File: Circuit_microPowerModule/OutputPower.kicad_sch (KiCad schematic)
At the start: 61 parts, among them J101 Screw_Terminal_01x02, J401 Conn_01x03, Q401 RU1C002ZP, Q402 RK7002BM, Q403 RU1C002ZP, Q404 RK7002BM, U301 OPA376xxDBV, U401 MP2315S, U407 L298N

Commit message: update system power circuit layout
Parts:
- C409, C410: footprint Capacitor_SMD:C_1206_3216Metric -> Capacitor_SMD:C_1210_3225Metric
- L402: footprint Inductor_SMD_Wurth:L_Wurth_WE-LQSH-2512 -> Inductor_SMD:L_Sunlord_MWSA1204S-4R7
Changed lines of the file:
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@@
       (effects (font (size 1.27 1.27)) (justify left))
     )
-    (property "Footprint" "Capacitor_SMD:C_1206_3216Metric" (at 144.78 71.12 0)
+    (property "Footprint" "Capacitor_SMD:C_1210_3225Metric" (at 144.78 71.12 0)
       (effects (font (size 1.27 1.27)) hide)
     )
@@
       (effects (font (size 1.27 1.27)))
     )
-    (property "Footprint" "Inductor_SMD_Wurth:L_Wurth_WE-LQSH-2512" (at 121.92 68.58 0)
+    (property "Footprint" "Inductor_SMD:L_Sunlord_MWSA1204S-4R7" (at 121.92 68.58 0)
       (effects (font (size 1.27 1.27)) hide)
     )
@@
       (effects (font (size 1.27 1.27)) (justify left))
     )
-    (property "Footprint" "Capacitor_SMD:C_1206_3216Metric" (at 128.27 71.12 0)
-      (effects (font (size 1.27 1.27)) hide)
-    )
+    (property "Footprint" "Capacitor_SMD:C_1210_3225Metric" (at 128.27 71.12 0)
+      (effects (font (size 1.27 1.27)) hide)
+    )

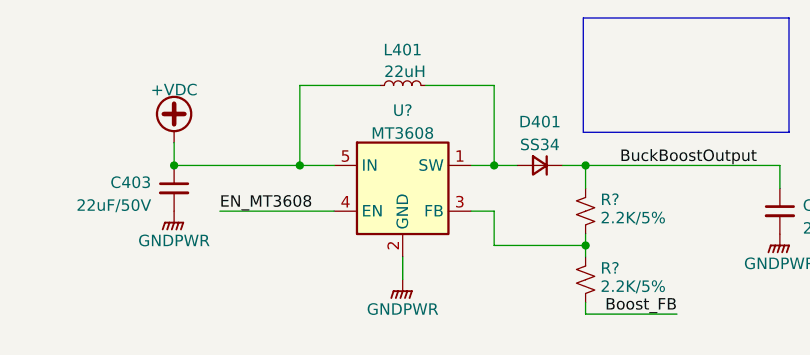
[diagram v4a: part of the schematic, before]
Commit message: update output inductor footprint
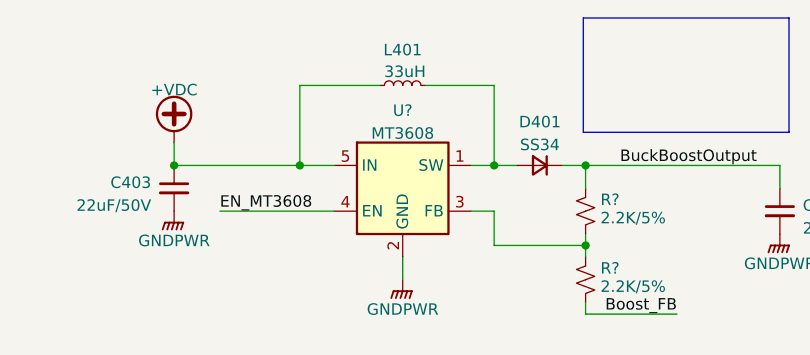
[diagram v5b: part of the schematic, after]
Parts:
- L401: value 22uH -> 33uH; footprint Inductor_SMD_Wurth:L_Wurth_WE-LQSH-2512 -> Inductor_SMD:L_Bourns-SRU1028_10.0x10.0mm
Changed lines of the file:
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@@
       (effects (font (size 1.27 1.27)))
     )
-    (property "Value" "22uH" (at 81.534 23.876 90)
+    (property "Value" "33uH" (at 81.534 23.876 90)
       (effects (font (size 1.27 1.27)))
     )
-    (property "Footprint" "Inductor_SMD_Wurth:L_Wurth_WE-LQSH-2512" (at 81.28 25.4 0)
+    (property "Footprint" "Inductor_SMD:L_Bourns-SRU1028_10.0x10.0mm" (at 81.28 25.4 0)
       (effects (font (size 1.27 1.27)) hide)
     )

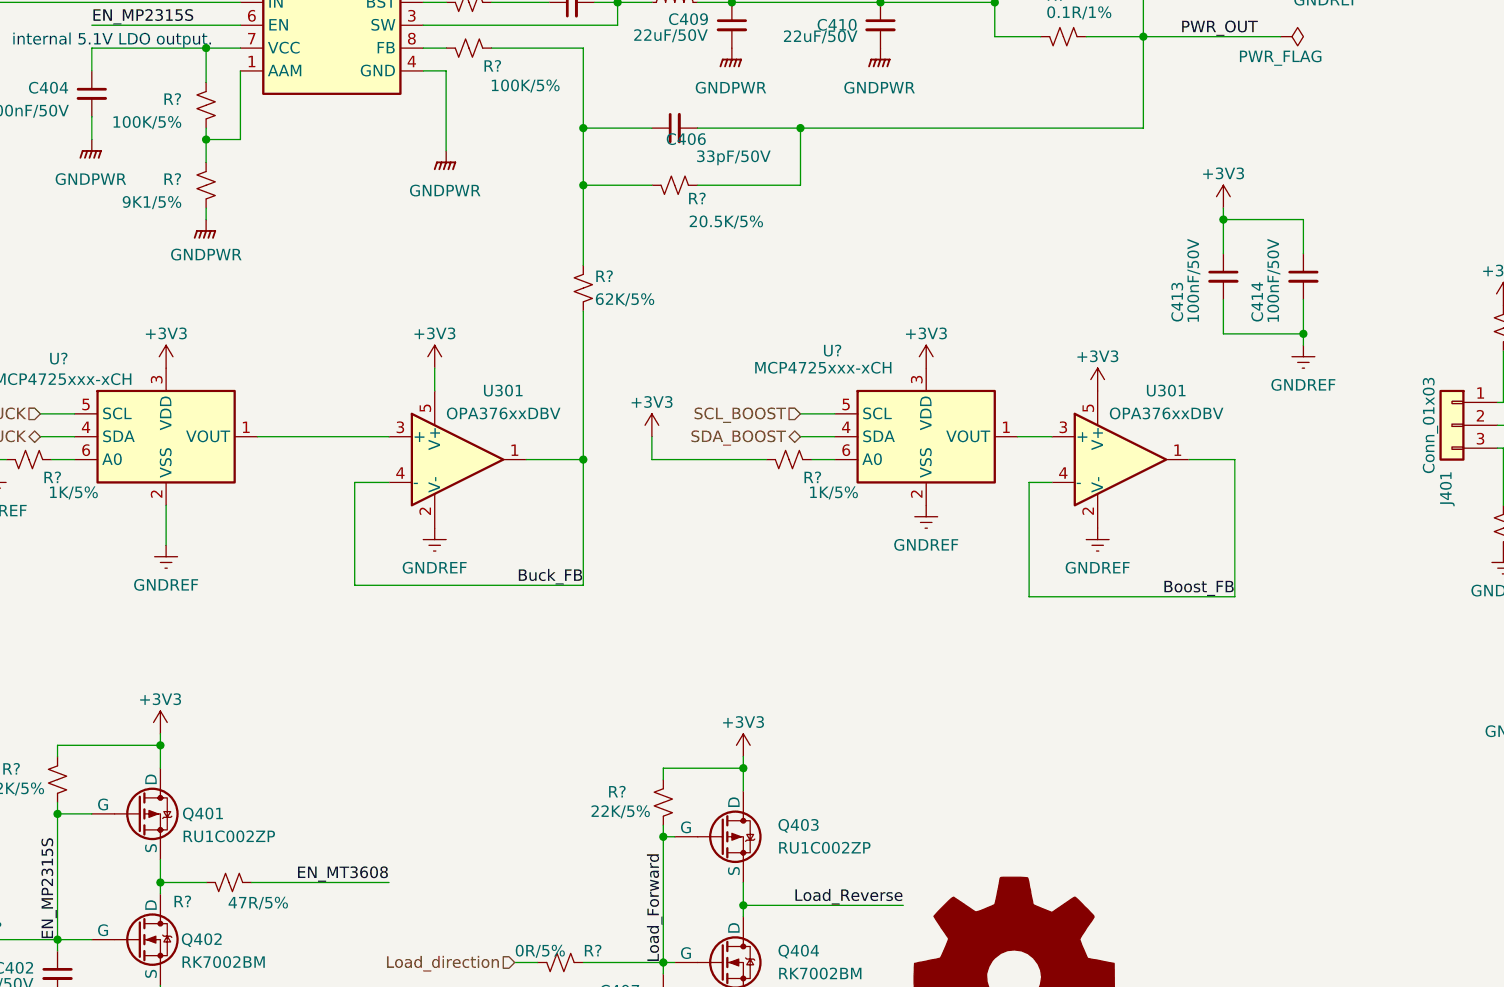
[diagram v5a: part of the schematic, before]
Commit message: modify DAC to Voltage follwers
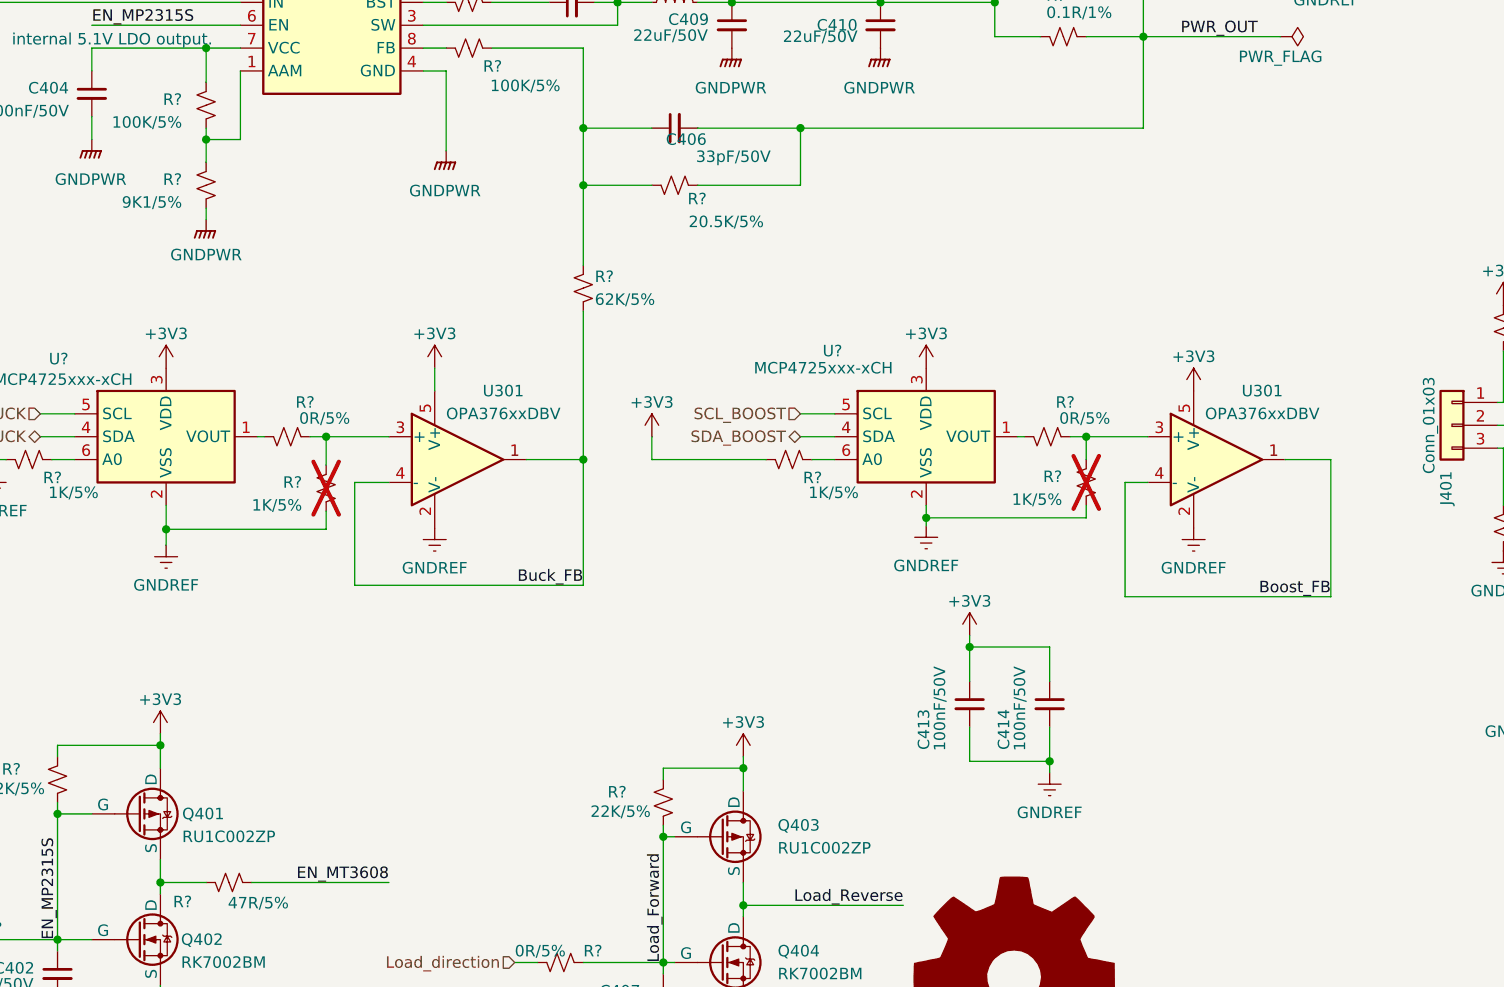
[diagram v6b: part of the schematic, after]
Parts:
- added R? (x2): 1K/5%, Resistor_SMD:R_0603_1608Metric, symbol Device:R_Small_US
- added R? (x2): 0R/5%, Resistor_SMD:R_0603_1608Metric, symbol Device:R_Small_US
- R?: footprint Resistor_SMD:R_0603_1608Metric -> Resistor_SMD:R_1206_3216Metric
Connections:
- net GNDREF: now also R?.1, R?.1
- net at U?.1 (VOUT): now also R?.2; no longer U301.3 (+)
- net at U301.3 (+): now also R?.1, R?.2; no longer U?.1 (VOUT)
- new net: R?.1, R?.2, U301.3 (+)
- new net: R?.2, U?.1 (VOUT)
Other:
- moved on the sheet: C413, C414, U301
